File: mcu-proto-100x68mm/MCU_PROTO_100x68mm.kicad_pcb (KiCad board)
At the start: 2 copper layers, 90 x 58 mm, 333 parts, among them J1 Screw_Terminal_01x04, J10 Conn_01x20_Female, J11 Conn_01x01_Male, J12 Conn_01x01_Male, J2 Screw_Terminal_01x04, J3 Conn_01x20_Female, J4 Conn_01x20_Female, J5 Conn_01x20_Female, J6 Conn_01x20_Female, J7 Conn_01x20_Female, J8 Conn_01x20_Female, J9 Conn_01x20_Female

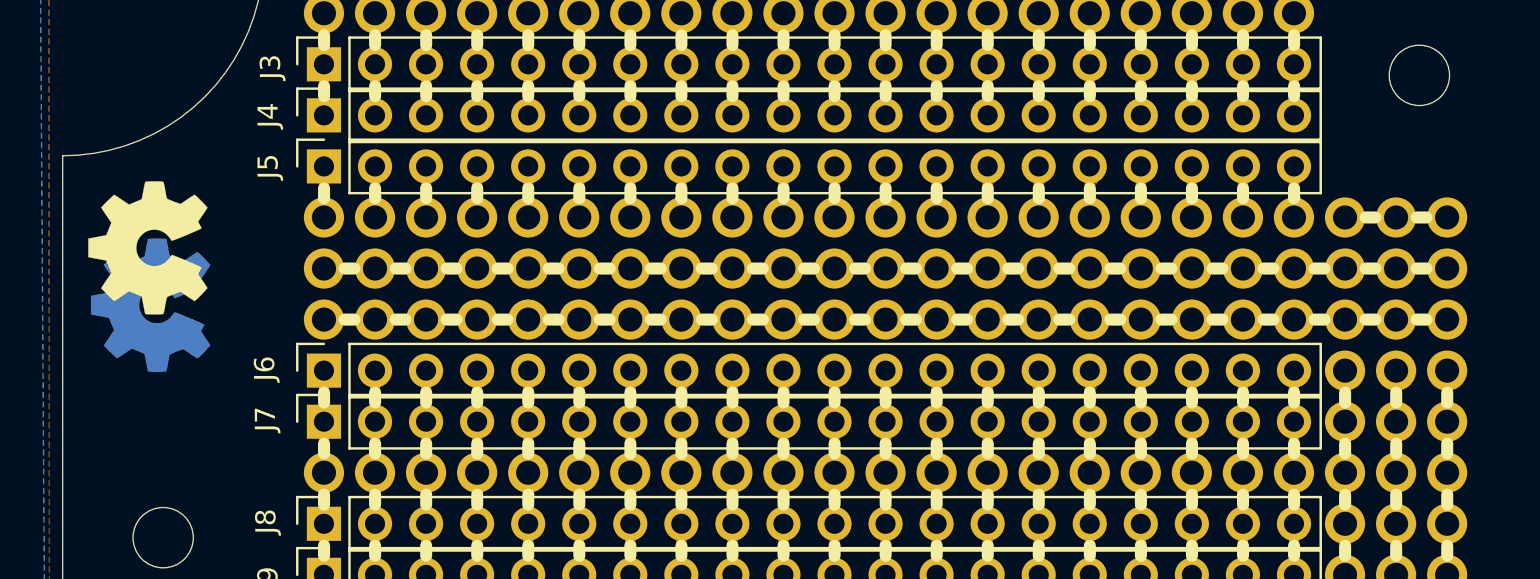
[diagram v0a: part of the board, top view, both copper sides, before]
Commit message: doc:(misistemote)changed name
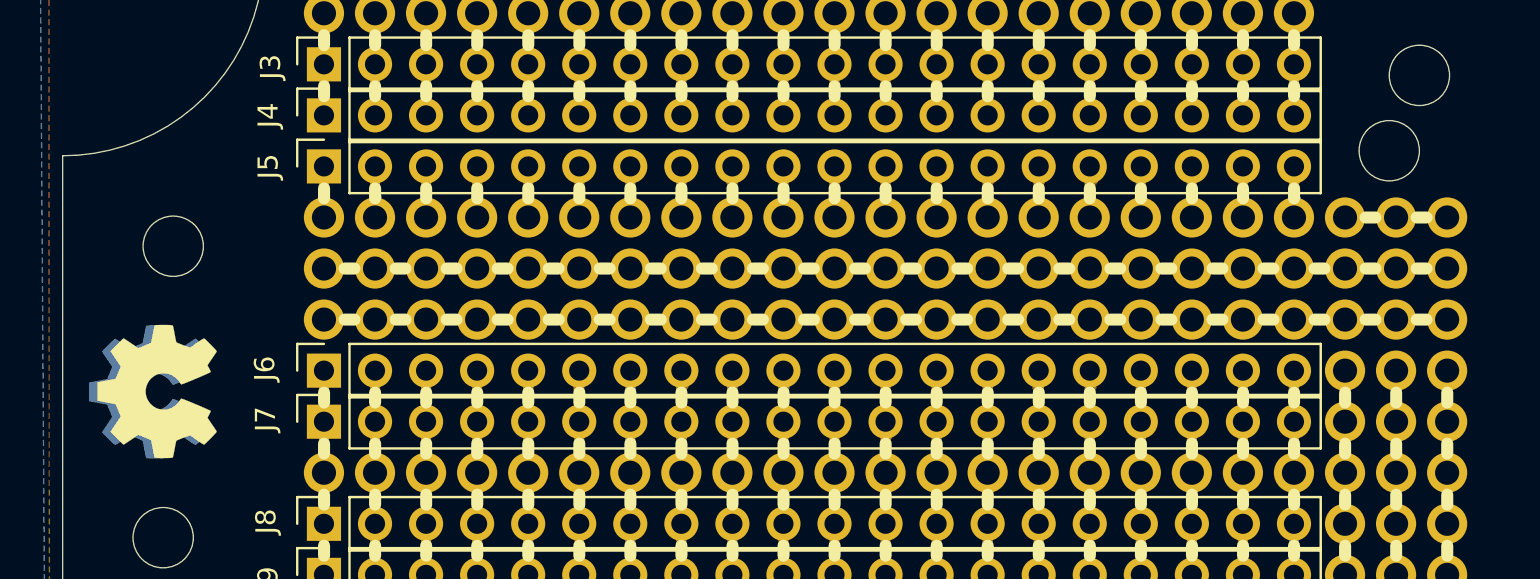
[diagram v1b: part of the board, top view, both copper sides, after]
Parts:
- added H2: MountingHole, MountingHole:MountingHole_3mm, F.Cu at (105.5, 114.5)
- added H4: MountingHole, MountingHole:MountingHole_3mm, F.Cu at (166.0, 109.8)
- moved REF** 7.16 mm to (104.7, 121.7)
- moved REF** 4.31 mm to (104.3, 121.7)
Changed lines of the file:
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@@
     (tracks 892)
     (zones 0)
-    (modules 333)
+    (modules 335)
     (nets 170)
   )
@@
     (uvia_drill 0.1)
   )
+  (module MountingHole:MountingHole_3mm (layer F.Cu)
+    (at 166 109.75)
+    (descr "Mounting Hole 3mm, no annular")
+    (tags "mounting hole 3mm no annular")
+    (attr virtual)
+    (fp_text reference H4 (at 0 -4) (layer F.SilkS) hide
+      (effects (font (size 1 1) (thickness 0.15)))
+    )
+    (fp_text value MountingHole (at 0 4) (layer F.Fab)
+      (effects (font (size 1 1) (thickness 0.15)))
+    )
+    (fp_text user %R (at 0.3 0) (layer F.Fab)
+      (effects (font (size 1 1) (thickness 0.15)))
+    )
+    (fp_circle (center 0 0) (end 3 0) (layer Cmts.User) (width 0.15))
+    (fp_circle (center 0 0) (end 3.25 0) (layer F.CrtYd) (width 0.05))
+    (pad 1 np_thru_hole circle (at 0 0) (size 3 3) (drill 3) (layers *.Cu *.Mask))
+  )
+  (module MountingHole:MountingHole_3mm (layer F.Cu)
+    (at 105.5 114.5)
+    (descr "Mounting Hole 3mm, no annular")
+    (tags "mounting hole 3mm no annular")
+    (attr virtual)
+    (fp_text reference H2 (at 0.545 2.5) (layer F.SilkS) hide
+      (effects (font (size 1 1) (thickness 0.15)))
+    )
+    (fp_text value MountingHole (at 0 4) (layer F.Fab)
+      (effects (font (size 1 1) (thickness 0.15)))
+    )
+    (fp_text user %R (at 0.3 0) (layer F.Fab)
+      (effects (font (size 1 1) (thickness 0.15)))
+    )
+    (fp_circle (center 0 0) (end 3 0) (layer Cmts.User) (width 0.15))
+    (fp_circle (center 0 0) (end 3.25 0) (layer F.CrtYd) (width 0.05))
+    (pad 1 np_thru_hole circle (at 0 0) (size 3 3) (drill 3) (layers *.Cu *.Mask))
+  )
   (module Connector_Wire:SolderWirePad_1x01_Drill0.8mm (layer F.Cu)
     (at 130.78 135.93)
@@
   )
   (module Symbol:OSHW-Symbol_6.7x6mm_SilkScreen (layer F.Cu)
-    (at 104.2543 114.5921 90)
+    (at 104.71912 121.73712 90)
     (descr "Open Source Hardware Symbol")
     (tags "Logo Symbol OSHW")
@@
   )
   (module Symbol:OSHW-Symbol_6.7x6mm_Copper (layer B.Cu)
-    (at 104.394 117.4242 270)
+    (at 104.30256 121.73712 270)
     (descr "Open Source Hardware Symbol")
     (tags "Logo Symbol OSHW")

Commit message: Minor revision update
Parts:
- removed H2 (x2), H3, H4 (x2), H5, H6: MountingHole, MountingHole:MountingHole_3mm
- removed J10, J5, J6, J7, J8, J9: Conn_01x20_Female, Connector_PinSocket_2.54mm:PinSocket_1x20_P2.54mm_Vertical
- removed J11, J12: Conn_01x01_Male, Connector_Wire:SolderWirePad_1x01_Drill0.8mm
- removed the REF** at (130.8, 135.9)
- removed the REF** at (140.9, 125.8)
- removed the REF** at (161.3, 151.2)
- removed the REF** at (158.7, 151.2)
- removed the REF** at (156.2, 151.2)
- removed the REF** at (153.6, 151.2)
- removed the REF** at (151.1, 151.2)
- removed the REF** at (148.6, 151.2)
- removed the REF** at (146.0, 151.2)
- removed the REF** at (143.5, 151.2)
- removed the REF** at (140.9, 151.2)
- removed the REF** at (138.4, 151.2)
- removed the REF** at (138.4, 125.8)
- removed the REF** at (135.9, 151.2)
- removed the REF** at (133.3, 151.2)
- removed the REF** at (130.8, 151.2)
- removed the REF** at (128.2, 151.2)
- removed the REF** at (161.3, 148.6)
- removed the REF** at (158.7, 148.6)
- removed the REF** at (156.2, 148.6)
- removed the REF** at (153.6, 148.6)
- removed the REF** at (151.1, 148.6)
- removed the REF** at (148.6, 148.6)
- removed the REF** at (135.9, 125.8)
- removed the REF** at (146.0, 148.6)
- removed the REF** at (143.5, 148.6)
- removed the REF** at (140.9, 148.6)
- removed the REF** at (138.4, 148.6)
- removed the REF** at (135.9, 148.6)
- removed the REF** at (133.3, 148.6)
- removed the REF** at (130.8, 148.6)
- removed the REF** at (128.2, 148.6)
- removed the REF** at (115.5, 156.2)
- removed the REF** at (113.0, 156.2)
- removed the REF** at (133.3, 125.8)
- removed the REF** at (115.5, 153.7)
- removed the REF** at (113.0, 153.7)
- removed the REF** at (115.5, 151.2)
- removed the REF** at (113.0, 151.2)
- removed the REF** at (115.5, 148.6)
- removed the REF** at (113.0, 148.6)
- removed the REF** at (161.3, 146.1)
- removed the REF** at (158.7, 146.1)
- removed the REF** at (156.2, 146.1)
- removed the REF** at (153.6, 146.1)
- removed the REF** at (130.8, 125.8)
- removed the REF** at (151.1, 146.1)
- removed the REF** at (148.6, 146.1)
- removed the REF** at (146.0, 146.1)
- removed the REF** at (143.5, 146.1)
- removed the REF** at (140.9, 146.1)
- removed the REF** at (138.4, 146.1)
- removed the REF** at (135.9, 146.1)
- removed the REF** at (133.3, 146.1)
- removed the REF** at (130.8, 146.1)
- removed the REF** at (128.2, 146.1)
- removed the REF** at (128.2, 125.8)
- removed the REF** at (125.7, 146.1)
- removed the REF** at (123.2, 146.1)
- removed the REF** at (120.6, 146.1)
- removed the REF** at (118.1, 146.1)
- removed the REF** at (115.5, 146.1)
- removed the REF** at (113.0, 146.1)
- removed the REF** at (161.3, 143.6)
- removed the REF** at (158.7, 143.6)
- removed the REF** at (156.2, 143.6)
- removed the REF** at (153.6, 143.6)
- removed the REF** at (125.7, 125.8)
- removed the REF** at (151.1, 143.6)
- removed the REF** at (148.6, 143.6)
- removed the REF** at (146.0, 143.6)
- removed the REF** at (143.5, 143.6)
- removed the REF** at (140.9, 143.6)
- removed the REF** at (138.4, 143.6)
- removed the REF** at (135.9, 143.6)
- removed the REF** at (133.3, 143.6)
- removed the REF** at (130.8, 143.6)
- removed the REF** at (128.2, 143.6)
- removed the REF** at (123.2, 125.8)
- removed the REF** at (125.7, 143.6)
- removed the REF** at (123.2, 143.6)
- removed the REF** at (120.6, 143.6)
- removed the REF** at (118.1, 143.6)
- removed the REF** at (115.5, 143.6)
- removed the REF** at (113.0, 143.6)
- removed the REF** at (161.3, 141.0)
- removed the REF** at (158.7, 141.0)
- removed the REF** at (156.2, 141.0)
- removed the REF** at (153.6, 141.0)
- removed the REF** at (120.6, 125.8)
- removed the REF** at (151.1, 141.0)
- removed the REF** at (148.6, 141.0)
- removed the REF** at (146.0, 141.0)
- removed the REF** at (143.5, 141.0)
- removed the REF** at (140.9, 141.0)
- removed the REF** at (138.4, 141.0)
- removed the REF** at (135.9, 141.0)
- removed the REF** at (133.3, 141.0)
- removed the REF** at (130.8, 141.0)
- removed the REF** at (128.2, 141.0)
- removed the REF** at (118.1, 125.8)
- removed the REF** at (125.7, 141.0)
- removed the REF** at (123.2, 141.0)
- removed the REF** at (120.6, 141.0)
- removed the REF** at (118.1, 141.0)
- removed the REF** at (115.5, 141.0)
- removed the REF** at (113.0, 141.0)
- removed the REF** at (161.3, 138.5)
- removed the REF** at (158.7, 138.5)
- removed the REF** at (156.2, 138.5)
- removed the REF** at (153.6, 138.5)
- removed the REF** at (161.3, 125.8)
- removed the REF** at (115.5, 125.8)
- removed the REF** at (151.1, 138.5)
- removed the REF** at (148.6, 138.5)
- removed the REF** at (146.0, 138.5)
- removed the REF** at (143.5, 138.5)
- removed the REF** at (140.9, 138.5)
- removed the REF** at (138.4, 138.5)
- removed the REF** at (135.9, 138.5)
- removed the REF** at (133.3, 138.5)
- removed the REF** at (130.8, 138.5)
- removed the REF** at (128.2, 138.5)
- removed the REF** at (113.0, 125.8)
- removed the REF** at (125.7, 138.5)
- removed the REF** at (123.2, 138.5)
- removed the REF** at (120.6, 138.5)
- removed the REF** at (118.1, 138.5)
- removed the REF** at (115.5, 138.5)
- removed the REF** at (113.0, 138.5)
- removed the REF** at (161.3, 135.9)
- removed the REF** at (158.7, 135.9)
- removed the REF** at (156.2, 135.9)
- removed the REF** at (153.6, 135.9)
- removed the REF** at (174.5, 121.5)
- removed the REF** at (151.1, 135.9)
- removed the REF** at (148.6, 135.9)
- removed the REF** at (146.0, 135.9)
- removed the REF** at (143.5, 135.9)
- removed the REF** at (140.9, 135.9)
- removed the REF** at (138.4, 135.9)
- removed the REF** at (135.9, 135.9)
- removed the REF** at (133.3, 135.9)
- removed the REF** at (128.2, 135.9)
- removed the REF** at (125.7, 135.9)
- removed the REF** at (174.5, 118.0)
- removed the REF** at (123.2, 135.9)
- removed the REF** at (120.6, 135.9)
- removed the REF** at (118.1, 135.9)
- removed the REF** at (115.5, 135.9)
- removed the REF** at (161.3, 118.2)
- removed the REF** at (158.7, 118.2)
- removed the REF** at (156.2, 118.2)
- removed the REF** at (153.6, 118.2)
- removed the REF** at (151.1, 118.2)
- removed the REF** at (148.6, 118.2)
- removed the REF** at (174.5, 114.5)
- removed the REF** at (146.0, 118.2)
- removed the REF** at (143.5, 118.2)
- removed the REF** at (140.9, 118.2)
- removed the REF** at (138.4, 118.2)
- removed the REF** at (135.9, 118.2)
- removed the REF** at (133.3, 118.2)
- removed the REF** at (130.8, 118.2)
- removed the REF** at (128.2, 118.2)
- removed the REF** at (125.7, 118.2)
- removed the REF** at (123.2, 118.2)
- removed the REF** at (174.5, 111.0)
- removed the REF** at (120.6, 118.2)
- removed the REF** at (118.1, 118.2)
- removed the REF** at (115.5, 118.2)
- removed the REF** at (113.0, 118.2)
- removed the REF** at (161.3, 115.6)
- removed the REF** at (158.7, 115.6)
- removed the REF** at (156.2, 115.6)
- removed the REF** at (153.6, 115.6)
- removed the REF** at (151.1, 115.6)
- removed the REF** at (148.6, 115.6)
- removed the REF** at (168.9, 133.4)
- removed the REF** at (146.0, 115.6)
- removed the REF** at (143.5, 115.6)
- removed the REF** at (140.9, 115.6)
- removed the REF** at (138.4, 115.6)
- removed the REF** at (135.9, 115.6)
- removed the REF** at (133.3, 115.6)
- removed the REF** at (130.8, 115.6)
- removed the REF** at (128.2, 115.6)
- removed the REF** at (125.7, 115.6)
- removed the REF** at (123.2, 115.6)
- removed the REF** at (166.3, 133.4)
- removed the REF** at (120.6, 115.6)
- removed the REF** at (118.1, 115.6)
- removed the REF** at (115.5, 115.6)
- removed the REF** at (113.0, 115.6)
- removed the REF** at (161.3, 113.1)
- removed the REF** at (158.7, 113.1)
- removed the REF** at (156.2, 113.1)
- removed the REF** at (153.6, 113.1)
- removed the REF** at (151.1, 113.1)
- removed the REF** at (148.6, 113.1)
- removed the REF** at (163.8, 133.4)
- removed the REF** at (146.0, 113.1)
- removed the REF** at (143.5, 113.1)
- removed the REF** at (140.9, 113.1)
- removed the REF** at (138.4, 113.1)
- removed the REF** at (135.9, 113.1)
- removed the REF** at (133.3, 113.1)
- removed the REF** at (130.8, 113.1)
- removed the REF** at (128.2, 113.1)
- removed the REF** at (125.7, 113.1)
- removed the REF** at (123.2, 113.1)
- removed the REF** at (168.9, 130.8)
- removed the REF** at (120.6, 113.1)
- removed the REF** at (118.1, 113.1)
- removed the REF** at (115.5, 113.1)
- removed the REF** at (113.0, 113.1)
- removed the REF** at (113.0, 135.9)
- removed the REF** at (113.0, 102.9)
- removed the REF** at (115.5, 102.9)
- removed the REF** at (118.1, 102.9)
- removed the REF** at (120.6, 102.9)
- removed the REF** at (123.2, 102.9)
- removed the REF** at (158.7, 125.8)
- removed the REF** at (166.3, 130.8)
- removed the REF** at (125.7, 102.9)
- removed the REF** at (148.6, 102.9)
- removed the REF** at (161.3, 102.9)
- removed the REF** at (158.7, 102.9)
- removed the REF** at (156.2, 102.9)
- removed the REF** at (153.6, 102.9)
- removed the REF** at (151.1, 102.9)
- removed the REF** at (146.0, 102.9)
- removed the REF** at (143.5, 102.9)
- removed the REF** at (140.9, 102.9)
- removed the REF** at (163.8, 130.8)
- removed the REF** at (138.4, 102.9)
- removed the REF** at (135.9, 102.9)
- removed the REF** at (133.3, 102.9)
- removed the REF** at (130.8, 102.9)
- removed the REF** at (128.2, 102.9)
- removed the REF** at (168.9, 128.3)
- removed the REF** at (166.3, 128.3)
- removed the REF** at (163.8, 128.3)
- removed the REF** at (168.9, 125.8)
- removed the REF** at (166.3, 125.8)
- removed the REF** at (163.8, 125.8)
- removed the REF** at (168.9, 123.2)
- removed the REF** at (166.3, 123.2)
- removed the REF** at (156.2, 125.8)
- removed the REF** at (163.8, 123.2)
- removed the REF** at (168.9, 120.7)
- removed the REF** at (166.3, 120.7)
- removed the REF** at (163.8, 120.7)
- removed the REF** at (168.9, 118.2)
- removed the REF** at (166.3, 118.2)
- removed the REF** at (163.8, 118.2)
- removed the REF** at (168.9, 115.6)
- removed the REF** at (166.3, 115.6)
- removed the REF** at (163.8, 115.6)
- removed the REF** at (153.6, 125.8)
- removed the REF** at (168.9, 113.1)
- removed the REF** at (166.3, 113.1)
- removed the REF** at (163.8, 113.1)
- removed the REF** at (174.5, 147.0)
- removed the REF** at (168.9, 146.1)
- removed the REF** at (166.3, 146.1)
- removed the REF** at (163.8, 146.1)
- removed the REF** at (174.5, 143.5)
- removed the REF** at (168.9, 143.6)
- removed the REF** at (166.3, 143.6)
- removed the REF** at (151.1, 125.8)
- removed the REF** at (163.8, 143.6)
- removed the REF** at (174.5, 140.0)
- removed the REF** at (168.9, 141.0)
- removed the REF** at (166.3, 141.0)
- removed the REF** at (163.8, 141.0)
- removed the REF** at (174.5, 136.5)
- removed the REF** at (168.9, 138.5)
- removed the REF** at (166.3, 138.5)
- removed the REF** at (163.8, 138.5)
- removed the REF** at (168.9, 135.9)
- removed the REF** at (148.6, 125.8)
- removed the REF** at (166.3, 135.9)
- removed the REF** at (163.8, 135.9)
- removed the REF** at (161.3, 156.2)
- removed the REF** at (158.7, 156.2)
- removed the REF** at (156.2, 156.2)
- removed the REF** at (153.6, 156.2)
- removed the REF** at (151.1, 156.2)
- removed the REF** at (148.6, 156.2)
- removed the REF** at (146.0, 156.2)
- removed the REF** at (143.5, 156.2)
- removed the REF** at (146.0, 125.8)
- removed the REF** at (140.9, 156.2)
- removed the REF** at (138.4, 156.2)
- removed the REF** at (135.9, 156.2)
- removed the REF** at (133.3, 156.2)
- removed the REF** at (130.8, 156.2)
- removed the REF** at (128.2, 156.2)
- removed the REF** at (161.3, 153.7)
- removed the REF** at (158.7, 153.7)
- removed the REF** at (156.2, 153.7)
- removed the REF** at (153.6, 153.7)
- removed the REF** at (143.5, 125.8)
- removed the REF** at (151.1, 153.7)
- removed the REF** at (148.6, 153.7)
- removed the REF** at (146.0, 153.7)
- removed the REF** at (143.5, 153.7)
- removed the REF** at (140.9, 153.7)
- removed the REF** at (138.4, 153.7)
- removed the REF** at (135.9, 153.7)
- removed the REF** at (133.3, 153.7)
- removed the REF** at (130.8, 153.7)
- removed the REF** at (128.2, 153.7)
- added REF**: Round_Pad_1.7mm_Hole_1.0mm, proto-pcb-pads:RoundPad_1.7mm_Hole_1.0mm, F.Cu at (130.8, 153.7)
- added REF**: Round_Pad_1.7mm_Hole_1.0mm, proto-pcb-pads:RoundPad_1.7mm_Hole_1.0mm, F.Cu at (118.1, 110.5)
- added REF**: Round_Pad_1.7mm_Hole_1.0mm, proto-pcb-pads:RoundPad_1.7mm_Hole_1.0mm, F.Cu at (158.7, 141.0)
- added REF**: Round_Pad_1.7mm_Hole_1.0mm, proto-pcb-pads:RoundPad_1.7mm_Hole_1.0mm, F.Cu at (153.6, 135.9)
- added REF**: Round_Pad_1.7mm_Hole_1.0mm, proto-pcb-pads:RoundPad_1.7mm_Hole_1.0mm, F.Cu at (163.8, 123.2)
- added REF**: Round_Pad_1.7mm_Hole_1.0mm, proto-pcb-pads:RoundPad_1.7mm_Hole_1.0mm, F.Cu at (125.7, 128.3)
- added REF**: Round_Pad_1.7mm_Hole_1.0mm, proto-pcb-pads:RoundPad_1.7mm_Hole_1.0mm, F.Cu at (148.6, 141.0)
- added REF**: Round_Pad_1.7mm_Hole_1.0mm, proto-pcb-pads:RoundPad_1.7mm_Hole_1.0mm, F.Cu at (153.6, 115.6)
- added REF**: Round_Pad_1.7mm_Hole_1.0mm, proto-pcb-pads:RoundPad_1.7mm_Hole_1.0mm, F.Cu at (143.5, 108.0)
- added REF**: Round_Pad_1.7mm_Hole_1.0mm, proto-pcb-pads:RoundPad_1.7mm_Hole_1.0mm, F.Cu at (161.3, 130.8)
- added REF**: Round_Pad_1.7mm_Hole_1.0mm, proto-pcb-pads:RoundPad_1.7mm_Hole_1.0mm, F.Cu at (115.5, 135.9)
- added REF**: Round_Pad_1.7mm_Hole_1.0mm, proto-pcb-pads:RoundPad_1.7mm_Hole_1.0mm, F.Cu at (153.6, 130.8)
- added REF**: Round_Pad_1.7mm_Hole_1.0mm, proto-pcb-pads:RoundPad_1.7mm_Hole_1.0mm, F.Cu at (133.3, 115.6)
- added REF**: Round_Pad_1.7mm_Hole_1.0mm, proto-pcb-pads:RoundPad_1.7mm_Hole_1.0mm, F.Cu at (120.6, 128.3)
- added REF**: Round_Pad_1.7mm_Hole_1.0mm, proto-pcb-pads:RoundPad_1.7mm_Hole_1.0mm, F.Cu at (130.8, 151.2)
- added REF**: Round_Pad_1.7mm_Hole_1.0mm, proto-pcb-pads:RoundPad_1.7mm_Hole_1.0mm, F.Cu at (130.8, 146.1)
- added REF**: Round_Pad_1.7mm_Hole_1.0mm, proto-pcb-pads:RoundPad_1.7mm_Hole_1.0mm, F.Cu at (146.0, 138.5)
- added REF**: Round_Pad_1.7mm_Hole_1.0mm, proto-pcb-pads:RoundPad_1.7mm_Hole_1.0mm, F.Cu at (143.5, 128.3)
- added REF**: Round_Pad_1.7mm_Hole_1.0mm, proto-pcb-pads:RoundPad_1.7mm_Hole_1.0mm, F.Cu at (146.0, 128.3)
- added REF**: Round_Pad_1.7mm_Hole_1.0mm, proto-pcb-pads:RoundPad_1.7mm_Hole_1.0mm, F.Cu at (140.9, 130.8)
- added REF**: Round_Pad_1.7mm_Hole_1.0mm, proto-pcb-pads:RoundPad_1.7mm_Hole_1.0mm, F.Cu at (115.5, 138.5)
- added REF**: Round_Pad_1.7mm_Hole_1.0mm, proto-pcb-pads:RoundPad_1.7mm_Hole_1.0mm, F.Cu at (113.0, 115.6)
- added REF**: Round_Pad_1.7mm_Hole_1.0mm, proto-pcb-pads:RoundPad_1.7mm_Hole_1.0mm, F.Cu at (163.8, 120.7)
- added REF**: Round_Pad_1.7mm_Hole_1.0mm, proto-pcb-pads:RoundPad_1.7mm_Hole_1.0mm, F.Cu at (140.9, 148.6)
- added REF**: Round_Pad_1.7mm_Hole_1.0mm, proto-pcb-pads:RoundPad_1.7mm_Hole_1.0mm, F.Cu at (133.3, 120.7)
- added REF**: Round_Pad_1.7mm_Hole_1.0mm, proto-pcb-pads:RoundPad_1.7mm_Hole_1.0mm, F.Cu at (113.0, 133.4)
- added REF**: Round_Pad_1.7mm_Hole_1.0mm, proto-pcb-pads:RoundPad_1.7mm_Hole_1.0mm, F.Cu at (125.7, 120.7)
- added REF**: Round_Pad_1.7mm_Hole_1.0mm, proto-pcb-pads:RoundPad_1.7mm_Hole_1.0mm, F.Cu at (151.1, 153.7)
- added REF**: Round_Pad_1.7mm_Hole_1.0mm, proto-pcb-pads:RoundPad_1.7mm_Hole_1.0mm, F.Cu at (125.7, 138.5)
- added REF**: Round_Pad_1.7mm_Hole_1.0mm, proto-pcb-pads:RoundPad_1.7mm_Hole_1.0mm, F.Cu at (130.8, 123.2)
- added REF**: Round_Pad_1.7mm_Hole_1.0mm, proto-pcb-pads:RoundPad_1.7mm_Hole_1.0mm, F.Cu at (128.2, 123.2)
- added REF**: Round_Pad_1.7mm_Hole_1.0mm, proto-pcb-pads:RoundPad_1.7mm_Hole_1.0mm, F.Cu at (174.5, 111.0)
- added REF**: Round_Pad_1.7mm_Hole_1.0mm, proto-pcb-pads:RoundPad_1.7mm_Hole_1.0mm, F.Cu at (133.3, 138.5)
- added REF**: Round_Pad_1.7mm_Hole_1.0mm, proto-pcb-pads:RoundPad_1.7mm_Hole_1.0mm, F.Cu at (161.3, 135.9)
- added REF**: Round_Pad_1.7mm_Hole_1.0mm, proto-pcb-pads:RoundPad_1.7mm_Hole_1.0mm, F.Cu at (133.3, 102.9)
- added REF**: Round_Pad_1.7mm_Hole_1.0mm, proto-pcb-pads:RoundPad_1.7mm_Hole_1.0mm, F.Cu at (123.2, 146.1)
- added REF**: Round_Pad_1.7mm_Hole_1.0mm, proto-pcb-pads:RoundPad_1.7mm_Hole_1.0mm, F.Cu at (138.4, 102.9)
- added REF**: Round_Pad_1.7mm_Hole_1.0mm, proto-pcb-pads:RoundPad_1.7mm_Hole_1.0mm, F.Cu at (146.0, 156.2)
- added REF**: Round_Pad_1.7mm_Hole_1.0mm, proto-pcb-pads:RoundPad_1.7mm_Hole_1.0mm, F.Cu at (123.2, 115.6)
- added REF**: Round_Pad_1.7mm_Hole_1.0mm, proto-pcb-pads:RoundPad_1.7mm_Hole_1.0mm, F.Cu at (151.1, 105.5)
- added REF**: Round_Pad_1.7mm_Hole_1.0mm, proto-pcb-pads:RoundPad_1.7mm_Hole_1.0mm, F.Cu at (123.2, 125.8)
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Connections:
- J1 pad 1: Net-(J1-Pad1) -> unconnected-(J1-Pin_1-Pad1)
- J1 pad 2: Net-(J1-Pad2) -> unconnected-(J1-Pin_2-Pad2)
- J1 pad 3: Net-(J1-Pad3) -> unconnected-(J1-Pin_3-Pad3)
- J1 pad 4: Net-(J1-Pad4) -> unconnected-(J1-Pin_4-Pad4)
- J2 pad 1: Net-(J2-Pad1) -> unconnected-(J2-Pin_1-Pad1)
- J2 pad 2: Net-(J2-Pad2) -> unconnected-(J2-Pin_2-Pad2)
- J2 pad 3: Net-(J2-Pad3) -> unconnected-(J2-Pin_3-Pad3)
- J2 pad 4: Net-(J2-Pad4) -> unconnected-(J2-Pin_4-Pad4)
- J3 pad 1: Net-(J3-Pad1) -> Net-(J3-Pin_1)
- J4 pad 1: Net-(J4-Pad1) -> Net-(J3-Pin_1)
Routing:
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- removed copper zone on B.Cu, net Net-(J11-Pad1)
- removed copper zone on F.Cu, net Net-(J11-Pad1)
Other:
- net class Default removed
- net class slimstack removed
- board text added: "GND"

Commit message: Silkscreen on front side
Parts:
- added REF**: Pad_Link_1.7mm_Width_1.0mm, proto-pcb-silks:PadLink_1.7mm_Width_1.0mm, F.Cu at (113.0, 105.5)
- added REF**1: Pad_Link_1.7mm_Width_1.0mm, proto-pcb-silks:PadLink_1.7mm_Width_1.0mm, F.Cu at (115.5, 105.5)
- added REF**10: Pad_Link_1.7mm_Width_1.0mm, proto-pcb-silks:PadLink_1.7mm_Width_1.0mm, F.Cu at (138.4, 105.5)
- added REF**100: Pad_Link_1.7mm_Width_1.0mm, proto-pcb-silks:PadLink_1.7mm_Width_1.0mm, F.Cu at (163.8, 118.2)
- added REF**101: Pad_Link_1.7mm_Width_1.0mm, proto-pcb-silks:PadLink_1.7mm_Width_1.0mm, F.Cu at (166.3, 118.2)
- added REF**102: Pad_Link_1.7mm_Width_1.0mm, proto-pcb-silks:PadLink_1.7mm_Width_1.0mm, F.Cu at (163.8, 113.1)
- added REF**103: Pad_Link_1.7mm_Width_1.0mm, proto-pcb-silks:PadLink_1.7mm_Width_1.0mm, F.Cu at (166.3, 113.1)
- added REF**104: Pad_Link_1.7mm_Width_1.0mm, proto-pcb-silks:PadLink_1.7mm_Width_1.0mm, F.Cu at (113.0, 123.2)
- added REF**105: Pad_Link_1.7mm_Width_1.0mm, proto-pcb-silks:PadLink_1.7mm_Width_1.0mm, F.Cu at (115.5, 123.2)
- added REF**106: Pad_Link_1.7mm_Width_1.0mm, proto-pcb-silks:PadLink_1.7mm_Width_1.0mm, F.Cu at (118.1, 123.2)
- added REF**107: Pad_Link_1.7mm_Width_1.0mm, proto-pcb-silks:PadLink_1.7mm_Width_1.0mm, F.Cu at (120.6, 123.2)
- added REF**108: Pad_Link_1.7mm_Width_1.0mm, proto-pcb-silks:PadLink_1.7mm_Width_1.0mm, F.Cu at (123.2, 123.2)
- added REF**109: Pad_Link_1.7mm_Width_1.0mm, proto-pcb-silks:PadLink_1.7mm_Width_1.0mm, F.Cu at (125.7, 123.2)
- added REF**11: Pad_Link_1.7mm_Width_1.0mm, proto-pcb-silks:PadLink_1.7mm_Width_1.0mm, F.Cu at (140.9, 105.5)
- added REF**110: Pad_Link_1.7mm_Width_1.0mm, proto-pcb-silks:PadLink_1.7mm_Width_1.0mm, F.Cu at (128.2, 123.2)
- added REF**111: Pad_Link_1.7mm_Width_1.0mm, proto-pcb-silks:PadLink_1.7mm_Width_1.0mm, F.Cu at (130.8, 123.2)
- added REF**112: Pad_Link_1.7mm_Width_1.0mm, proto-pcb-silks:PadLink_1.7mm_Width_1.0mm, F.Cu at (133.3, 123.2)
- added REF**113: Pad_Link_1.7mm_Width_1.0mm, proto-pcb-silks:PadLink_1.7mm_Width_1.0mm, F.Cu at (135.9, 123.2)
- added REF**114: Pad_Link_1.7mm_Width_1.0mm, proto-pcb-silks:PadLink_1.7mm_Width_1.0mm, F.Cu at (138.4, 123.2)
- added REF**115: Pad_Link_1.7mm_Width_1.0mm, proto-pcb-silks:PadLink_1.7mm_Width_1.0mm, F.Cu at (140.9, 123.2)
- added REF**116: Pad_Link_1.7mm_Width_1.0mm, proto-pcb-silks:PadLink_1.7mm_Width_1.0mm, F.Cu at (143.5, 123.2)
- added REF**117: Pad_Link_1.7mm_Width_1.0mm, proto-pcb-silks:PadLink_1.7mm_Width_1.0mm, F.Cu at (146.0, 123.2)
- added REF**118: Pad_Link_1.7mm_Width_1.0mm, proto-pcb-silks:PadLink_1.7mm_Width_1.0mm, F.Cu at (148.6, 123.2)
- added REF**119: Pad_Link_1.7mm_Width_1.0mm, proto-pcb-silks:PadLink_1.7mm_Width_1.0mm, F.Cu at (151.1, 123.2)
- added REF**12: Pad_Link_1.7mm_Width_1.0mm, proto-pcb-silks:PadLink_1.7mm_Width_1.0mm, F.Cu at (143.5, 105.5)
- added REF**120: Pad_Link_1.7mm_Width_1.0mm, proto-pcb-silks:PadLink_1.7mm_Width_1.0mm, F.Cu at (153.6, 123.2)
- added REF**121: Pad_Link_1.7mm_Width_1.0mm, proto-pcb-silks:PadLink_1.7mm_Width_1.0mm, F.Cu at (156.2, 123.2)
- added REF**122: Pad_Link_1.7mm_Width_1.0mm, proto-pcb-silks:PadLink_1.7mm_Width_1.0mm, F.Cu at (158.7, 123.2)
- added REF**123: Pad_Link_1.7mm_Width_1.0mm, proto-pcb-silks:PadLink_1.7mm_Width_1.0mm, F.Cu at (161.3, 123.2)
- added REF**124: Pad_Link_1.7mm_Width_1.0mm, proto-pcb-silks:PadLink_1.7mm_Width_1.0mm, F.Cu at (163.8, 123.2)
- added REF**125: Pad_Link_1.7mm_Width_1.0mm, proto-pcb-silks:PadLink_1.7mm_Width_1.0mm, F.Cu at (166.3, 123.2)
- added REF**126: Pad_Link_1.7mm_Width_1.0mm, proto-pcb-silks:PadLink_1.7mm_Width_1.0mm, F.Cu at (168.9, 123.2)
- added REF**127: Pad_Link_1.7mm_Width_1.0mm, proto-pcb-silks:PadLink_1.7mm_Width_1.0mm, F.Cu at (113.0, 125.8)
- added REF**128: Pad_Link_1.7mm_Width_1.0mm, proto-pcb-silks:PadLink_1.7mm_Width_1.0mm, F.Cu at (115.5, 125.8)
- added REF**129: Pad_Link_1.7mm_Width_1.0mm, proto-pcb-silks:PadLink_1.7mm_Width_1.0mm, F.Cu at (118.1, 125.8)
- added REF**13: Pad_Link_1.7mm_Width_1.0mm, proto-pcb-silks:PadLink_1.7mm_Width_1.0mm, F.Cu at (146.0, 105.5)
- added REF**130: Pad_Link_1.7mm_Width_1.0mm, proto-pcb-silks:PadLink_1.7mm_Width_1.0mm, F.Cu at (120.6, 125.8)
- added REF**131: Pad_Link_1.7mm_Width_1.0mm, proto-pcb-silks:PadLink_1.7mm_Width_1.0mm, F.Cu at (123.2, 125.8)
- added REF**132: Pad_Link_1.7mm_Width_1.0mm, proto-pcb-silks:PadLink_1.7mm_Width_1.0mm, F.Cu at (125.7, 125.8)
- added REF**133: Pad_Link_1.7mm_Width_1.0mm, proto-pcb-silks:PadLink_1.7mm_Width_1.0mm, F.Cu at (128.2, 125.8)
- added REF**134: Pad_Link_1.7mm_Width_1.0mm, proto-pcb-silks:PadLink_1.7mm_Width_1.0mm, F.Cu at (130.8, 125.8)
- added REF**135: Pad_Link_1.7mm_Width_1.0mm, proto-pcb-silks:PadLink_1.7mm_Width_1.0mm, F.Cu at (133.3, 125.8)
- added REF**136: Pad_Link_1.7mm_Width_1.0mm, proto-pcb-silks:PadLink_1.7mm_Width_1.0mm, F.Cu at (135.9, 125.8)
- added REF**137: Pad_Link_1.7mm_Width_1.0mm, proto-pcb-silks:PadLink_1.7mm_Width_1.0mm, F.Cu at (138.4, 125.8)
- added REF**138: Pad_Link_1.7mm_Width_1.0mm, proto-pcb-silks:PadLink_1.7mm_Width_1.0mm, F.Cu at (140.9, 125.8)
- added REF**139: Pad_Link_1.7mm_Width_1.0mm, proto-pcb-silks:PadLink_1.7mm_Width_1.0mm, F.Cu at (143.5, 125.8)
- added REF**14: Pad_Link_1.7mm_Width_1.0mm, proto-pcb-silks:PadLink_1.7mm_Width_1.0mm, F.Cu at (148.6, 105.5)
- added REF**140: Pad_Link_1.7mm_Width_1.0mm, proto-pcb-silks:PadLink_1.7mm_Width_1.0mm, F.Cu at (146.0, 125.8)
- added REF**141: Pad_Link_1.7mm_Width_1.0mm, proto-pcb-silks:PadLink_1.7mm_Width_1.0mm, F.Cu at (148.6, 125.8)
- added REF**142: Pad_Link_1.7mm_Width_1.0mm, proto-pcb-silks:PadLink_1.7mm_Width_1.0mm, F.Cu at (151.1, 125.8)
- added REF**143: Pad_Link_1.7mm_Width_1.0mm, proto-pcb-silks:PadLink_1.7mm_Width_1.0mm, F.Cu at (153.6, 125.8)
- added REF**144: Pad_Link_1.7mm_Width_1.0mm, proto-pcb-silks:PadLink_1.7mm_Width_1.0mm, F.Cu at (156.2, 125.8)
- added REF**145: Pad_Link_1.7mm_Width_1.0mm, proto-pcb-silks:PadLink_1.7mm_Width_1.0mm, F.Cu at (158.7, 125.8)
- added REF**146: Pad_Link_1.7mm_Width_1.0mm, proto-pcb-silks:PadLink_1.7mm_Width_1.0mm, F.Cu at (161.3, 125.8)
- added REF**147: Pad_Link_1.7mm_Width_1.0mm, proto-pcb-silks:PadLink_1.7mm_Width_1.0mm, F.Cu at (163.8, 125.8)
- added REF**148: Pad_Link_1.7mm_Width_1.0mm, proto-pcb-silks:PadLink_1.7mm_Width_1.0mm, F.Cu at (166.3, 125.8)
- added REF**149: Pad_Link_1.7mm_Width_1.0mm, proto-pcb-silks:PadLink_1.7mm_Width_1.0mm, F.Cu at (168.9, 125.8)
- added REF**15: Pad_Link_1.7mm_Width_1.0mm, proto-pcb-silks:PadLink_1.7mm_Width_1.0mm, F.Cu at (151.1, 105.5)
- added REF**150: Pad_Link_1.7mm_Width_1.0mm, proto-pcb-silks:PadLink_1.7mm_Width_1.0mm, F.Cu at (113.0, 128.3)
- added REF**151: Pad_Link_1.7mm_Width_1.0mm, proto-pcb-silks:PadLink_1.7mm_Width_1.0mm, F.Cu at (115.5, 128.3)
- added REF**152: Pad_Link_1.7mm_Width_1.0mm, proto-pcb-silks:PadLink_1.7mm_Width_1.0mm, F.Cu at (118.1, 128.3)
- added REF**153: Pad_Link_1.7mm_Width_1.0mm, proto-pcb-silks:PadLink_1.7mm_Width_1.0mm, F.Cu at (120.6, 128.3)
- added REF**154: Pad_Link_1.7mm_Width_1.0mm, proto-pcb-silks:PadLink_1.7mm_Width_1.0mm, F.Cu at (123.2, 128.3)
- added REF**155: Pad_Link_1.7mm_Width_1.0mm, proto-pcb-silks:PadLink_1.7mm_Width_1.0mm, F.Cu at (125.7, 128.3)
- added REF**156: Pad_Link_1.7mm_Width_1.0mm, proto-pcb-silks:PadLink_1.7mm_Width_1.0mm, F.Cu at (128.2, 128.3)
- added REF**157: Pad_Link_1.7mm_Width_1.0mm, proto-pcb-silks:PadLink_1.7mm_Width_1.0mm, F.Cu at (130.8, 128.3)
- added REF**158: Pad_Link_1.7mm_Width_1.0mm, proto-pcb-silks:PadLink_1.7mm_Width_1.0mm, F.Cu at (133.3, 128.3)
- added REF**159: Pad_Link_1.7mm_Width_1.0mm, proto-pcb-silks:PadLink_1.7mm_Width_1.0mm, F.Cu at (135.9, 128.3)
- added REF**16: Pad_Link_1.7mm_Width_1.0mm, proto-pcb-silks:PadLink_1.7mm_Width_1.0mm, F.Cu at (153.6, 105.5)
- added REF**160: Pad_Link_1.7mm_Width_1.0mm, proto-pcb-silks:PadLink_1.7mm_Width_1.0mm, F.Cu at (138.4, 128.3)
- added REF**161: Pad_Link_1.7mm_Width_1.0mm, proto-pcb-silks:PadLink_1.7mm_Width_1.0mm, F.Cu at (140.9, 128.3)
- added REF**162: Pad_Link_1.7mm_Width_1.0mm, proto-pcb-silks:PadLink_1.7mm_Width_1.0mm, F.Cu at (143.5, 128.3)
- added REF**163: Pad_Link_1.7mm_Width_1.0mm, proto-pcb-silks:PadLink_1.7mm_Width_1.0mm, F.Cu at (146.0, 128.3)
- added REF**164: Pad_Link_1.7mm_Width_1.0mm, proto-pcb-silks:PadLink_1.7mm_Width_1.0mm, F.Cu at (148.6, 128.3)
- added REF**165: Pad_Link_1.7mm_Width_1.0mm, proto-pcb-silks:PadLink_1.7mm_Width_1.0mm, F.Cu at (151.1, 128.3)
- added REF**166: Pad_Link_1.7mm_Width_1.0mm, proto-pcb-silks:PadLink_1.7mm_Width_1.0mm, F.Cu at (153.6, 128.3)
- added REF**167: Pad_Link_1.7mm_Width_1.0mm, proto-pcb-silks:PadLink_1.7mm_Width_1.0mm, F.Cu at (156.2, 128.3)
- added REF**168: Pad_Link_1.7mm_Width_1.0mm, proto-pcb-silks:PadLink_1.7mm_Width_1.0mm, F.Cu at (158.7, 128.3)
- added REF**169: Pad_Link_1.7mm_Width_1.0mm, proto-pcb-silks:PadLink_1.7mm_Width_1.0mm, F.Cu at (161.3, 128.3)
- added REF**17: Pad_Link_1.7mm_Width_1.0mm, proto-pcb-silks:PadLink_1.7mm_Width_1.0mm, F.Cu at (156.2, 105.5)
- added REF**170: Pad_Link_1.7mm_Width_1.0mm, proto-pcb-silks:PadLink_1.7mm_Width_1.0mm, F.Cu at (163.8, 128.3)
- added REF**171: Pad_Link_1.7mm_Width_1.0mm, proto-pcb-silks:PadLink_1.7mm_Width_1.0mm, F.Cu at (166.3, 128.3)
- added REF**172: Pad_Link_1.7mm_Width_1.0mm, proto-pcb-silks:PadLink_1.7mm_Width_1.0mm, F.Cu at (168.9, 128.3)
- added REF**173: Pad_Link_1.7mm_Width_1.0mm, proto-pcb-silks:PadLink_1.7mm_Width_1.0mm, F.Cu at (113.0, 130.8)
- added REF**174: Pad_Link_1.7mm_Width_1.0mm, proto-pcb-silks:PadLink_1.7mm_Width_1.0mm, F.Cu at (115.5, 130.8)
- added REF**175: Pad_Link_1.7mm_Width_1.0mm, proto-pcb-silks:PadLink_1.7mm_Width_1.0mm, F.Cu at (118.1, 130.8)
- added REF**176: Pad_Link_1.7mm_Width_1.0mm, proto-pcb-silks:PadLink_1.7mm_Width_1.0mm, F.Cu at (120.6, 130.8)
- added REF**177: Pad_Link_1.7mm_Width_1.0mm, proto-pcb-silks:PadLink_1.7mm_Width_1.0mm, F.Cu at (123.2, 130.8)
- added REF**178: Pad_Link_1.7mm_Width_1.0mm, proto-pcb-silks:PadLink_1.7mm_Width_1.0mm, F.Cu at (125.7, 130.8)
- added REF**179: Pad_Link_1.7mm_Width_1.0mm, proto-pcb-silks:PadLink_1.7mm_Width_1.0mm, F.Cu at (128.2, 130.8)
- added REF**18: Pad_Link_1.7mm_Width_1.0mm, proto-pcb-silks:PadLink_1.7mm_Width_1.0mm, F.Cu at (158.7, 105.5)
- added REF**180: Pad_Link_1.7mm_Width_1.0mm, proto-pcb-silks:PadLink_1.7mm_Width_1.0mm, F.Cu at (130.8, 130.8)
- added REF**181: Pad_Link_1.7mm_Width_1.0mm, proto-pcb-silks:PadLink_1.7mm_Width_1.0mm, F.Cu at (133.3, 130.8)
- added REF**182: Pad_Link_1.7mm_Width_1.0mm, proto-pcb-silks:PadLink_1.7mm_Width_1.0mm, F.Cu at (135.9, 130.8)
- added REF**183: Pad_Link_1.7mm_Width_1.0mm, proto-pcb-silks:PadLink_1.7mm_Width_1.0mm, F.Cu at (138.4, 130.8)
- added REF**184: Pad_Link_1.7mm_Width_1.0mm, proto-pcb-silks:PadLink_1.7mm_Width_1.0mm, F.Cu at (140.9, 130.8)
- added REF**185: Pad_Link_1.7mm_Width_1.0mm, proto-pcb-silks:PadLink_1.7mm_Width_1.0mm, F.Cu at (143.5, 130.8)
- added REF**186: Pad_Link_1.7mm_Width_1.0mm, proto-pcb-silks:PadLink_1.7mm_Width_1.0mm, F.Cu at (146.0, 130.8)
- added REF**187: Pad_Link_1.7mm_Width_1.0mm, proto-pcb-silks:PadLink_1.7mm_Width_1.0mm, F.Cu at (148.6, 130.8)
- added REF**188: Pad_Link_1.7mm_Width_1.0mm, proto-pcb-silks:PadLink_1.7mm_Width_1.0mm, F.Cu at (151.1, 130.8)
- added REF**189: Pad_Link_1.7mm_Width_1.0mm, proto-pcb-silks:PadLink_1.7mm_Width_1.0mm, F.Cu at (153.6, 130.8)
- added REF**19: Pad_Link_1.7mm_Width_1.0mm, proto-pcb-silks:PadLink_1.7mm_Width_1.0mm, F.Cu at (161.3, 105.5)
- added REF**190: Pad_Link_1.7mm_Width_1.0mm, proto-pcb-silks:PadLink_1.7mm_Width_1.0mm, F.Cu at (156.2, 130.8)
- added REF**191: Pad_Link_1.7mm_Width_1.0mm, proto-pcb-silks:PadLink_1.7mm_Width_1.0mm, F.Cu at (158.7, 130.8)
- added REF**192: Pad_Link_1.7mm_Width_1.0mm, proto-pcb-silks:PadLink_1.7mm_Width_1.0mm, F.Cu at (161.3, 130.8)
- added REF**193: Pad_Link_1.7mm_Width_1.0mm, proto-pcb-silks:PadLink_1.7mm_Width_1.0mm, F.Cu at (163.8, 130.8)
- added REF**194: Pad_Link_1.7mm_Width_1.0mm, proto-pcb-silks:PadLink_1.7mm_Width_1.0mm, F.Cu at (166.3, 130.8)
- added REF**195: Pad_Link_1.7mm_Width_1.0mm, proto-pcb-silks:PadLink_1.7mm_Width_1.0mm, F.Cu at (168.9, 130.8)
- added REF**196: Pad_Link_1.7mm_Width_1.0mm, proto-pcb-silks:PadLink_1.7mm_Width_1.0mm, F.Cu at (113.0, 133.4)
- added REF**197: Pad_Link_1.7mm_Width_1.0mm, proto-pcb-silks:PadLink_1.7mm_Width_1.0mm, F.Cu at (115.5, 133.4)
- added REF**198: Pad_Link_1.7mm_Width_1.0mm, proto-pcb-silks:PadLink_1.7mm_Width_1.0mm, F.Cu at (118.1, 133.4)
- added REF**199: Pad_Link_1.7mm_Width_1.0mm, proto-pcb-silks:PadLink_1.7mm_Width_1.0mm, F.Cu at (120.6, 133.4)
- added REF**2: Pad_Link_1.7mm_Width_1.0mm, proto-pcb-silks:PadLink_1.7mm_Width_1.0mm, F.Cu at (118.1, 105.5)
- added REF**20: Pad_Link_1.7mm_Width_1.0mm, proto-pcb-silks:PadLink_1.7mm_Width_1.0mm, F.Cu at (113.0, 108.0)
- added REF**200: Pad_Link_1.7mm_Width_1.0mm, proto-pcb-silks:PadLink_1.7mm_Width_1.0mm, F.Cu at (123.2, 133.4)
- added REF**201: Pad_Link_1.7mm_Width_1.0mm, proto-pcb-silks:PadLink_1.7mm_Width_1.0mm, F.Cu at (125.7, 133.4)
- added REF**202: Pad_Link_1.7mm_Width_1.0mm, proto-pcb-silks:PadLink_1.7mm_Width_1.0mm, F.Cu at (128.2, 133.4)
- added REF**203: Pad_Link_1.7mm_Width_1.0mm, proto-pcb-silks:PadLink_1.7mm_Width_1.0mm, F.Cu at (130.8, 133.4)
- added REF**204: Pad_Link_1.7mm_Width_1.0mm, proto-pcb-silks:PadLink_1.7mm_Width_1.0mm, F.Cu at (133.3, 133.4)
- added REF**205: Pad_Link_1.7mm_Width_1.0mm, proto-pcb-silks:PadLink_1.7mm_Width_1.0mm, F.Cu at (135.9, 133.4)
- added REF**206: Pad_Link_1.7mm_Width_1.0mm, proto-pcb-silks:PadLink_1.7mm_Width_1.0mm, F.Cu at (138.4, 133.4)
- added REF**207: Pad_Link_1.7mm_Width_1.0mm, proto-pcb-silks:PadLink_1.7mm_Width_1.0mm, F.Cu at (140.9, 133.4)
- added REF**208: Pad_Link_1.7mm_Width_1.0mm, proto-pcb-silks:PadLink_1.7mm_Width_1.0mm, F.Cu at (143.5, 133.4)
- added REF**209: Pad_Link_1.7mm_Width_1.0mm, proto-pcb-silks:PadLink_1.7mm_Width_1.0mm, F.Cu at (146.0, 133.4)
- added REF**21: Pad_Link_1.7mm_Width_1.0mm, proto-pcb-silks:PadLink_1.7mm_Width_1.0mm, F.Cu at (115.5, 108.0)
- added REF**210: Pad_Link_1.7mm_Width_1.0mm, proto-pcb-silks:PadLink_1.7mm_Width_1.0mm, F.Cu at (148.6, 133.4)
- added REF**211: Pad_Link_1.7mm_Width_1.0mm, proto-pcb-silks:PadLink_1.7mm_Width_1.0mm, F.Cu at (151.1, 133.4)
- added REF**212: Pad_Link_1.7mm_Width_1.0mm, proto-pcb-silks:PadLink_1.7mm_Width_1.0mm, F.Cu at (153.6, 133.4)
- added REF**213: Pad_Link_1.7mm_Width_1.0mm, proto-pcb-silks:PadLink_1.7mm_Width_1.0mm, F.Cu at (156.2, 133.4)
- added REF**214: Pad_Link_1.7mm_Width_1.0mm, proto-pcb-silks:PadLink_1.7mm_Width_1.0mm, F.Cu at (158.7, 133.4)
- added REF**215: Pad_Link_1.7mm_Width_1.0mm, proto-pcb-silks:PadLink_1.7mm_Width_1.0mm, F.Cu at (161.3, 133.4)
- added REF**216: Pad_Link_1.7mm_Width_1.0mm, proto-pcb-silks:PadLink_1.7mm_Width_1.0mm, F.Cu at (163.8, 133.4)
- added REF**217: Pad_Link_1.7mm_Width_1.0mm, proto-pcb-silks:PadLink_1.7mm_Width_1.0mm, F.Cu at (166.3, 133.4)
- added REF**218: Pad_Link_1.7mm_Width_1.0mm, proto-pcb-silks:PadLink_1.7mm_Width_1.0mm, F.Cu at (168.9, 133.4)
- added REF**219: Pad_Link_1.7mm_Width_1.0mm, proto-pcb-silks:PadLink_1.7mm_Width_1.0mm, F.Cu at (113.0, 135.9)
- added REF**22: Pad_Link_1.7mm_Width_1.0mm, proto-pcb-silks:PadLink_1.7mm_Width_1.0mm, F.Cu at (118.1, 108.0)
- added REF**220: Pad_Link_1.7mm_Width_1.0mm, proto-pcb-silks:PadLink_1.7mm_Width_1.0mm, F.Cu at (115.5, 135.9)
- added REF**221: Pad_Link_1.7mm_Width_1.0mm, proto-pcb-silks:PadLink_1.7mm_Width_1.0mm, F.Cu at (118.1, 135.9)
- added REF**222: Pad_Link_1.7mm_Width_1.0mm, proto-pcb-silks:PadLink_1.7mm_Width_1.0mm, F.Cu at (120.6, 135.9)
- added REF**223: Pad_Link_1.7mm_Width_1.0mm, proto-pcb-silks:PadLink_1.7mm_Width_1.0mm, F.Cu at (123.2, 135.9)
- added REF**224: Pad_Link_1.7mm_Width_1.0mm, proto-pcb-silks:PadLink_1.7mm_Width_1.0mm, F.Cu at (125.7, 135.9)
- added REF**225: Pad_Link_1.7mm_Width_1.0mm, proto-pcb-silks:PadLink_1.7mm_Width_1.0mm, F.Cu at (128.2, 135.9)
- added REF**226: Pad_Link_1.7mm_Width_1.0mm, proto-pcb-silks:PadLink_1.7mm_Width_1.0mm, F.Cu at (130.8, 135.9)
- added REF**227: Pad_Link_1.7mm_Width_1.0mm, proto-pcb-silks:PadLink_1.7mm_Width_1.0mm, F.Cu at (133.3, 135.9)
- added REF**228: Pad_Link_1.7mm_Width_1.0mm, proto-pcb-silks:PadLink_1.7mm_Width_1.0mm, F.Cu at (135.9, 135.9)
- added REF**229: Pad_Link_1.7mm_Width_1.0mm, proto-pcb-silks:PadLink_1.7mm_Width_1.0mm, F.Cu at (138.4, 135.9)
- added REF**23: Pad_Link_1.7mm_Width_1.0mm, proto-pcb-silks:PadLink_1.7mm_Width_1.0mm, F.Cu at (120.6, 108.0)
- added REF**230: Pad_Link_1.7mm_Width_1.0mm, proto-pcb-silks:PadLink_1.7mm_Width_1.0mm, F.Cu at (140.9, 135.9)
- added REF**231: Pad_Link_1.7mm_Width_1.0mm, proto-pcb-silks:PadLink_1.7mm_Width_1.0mm, F.Cu at (143.5, 135.9)
- added REF**232: Pad_Link_1.7mm_Width_1.0mm, proto-pcb-silks:PadLink_1.7mm_Width_1.0mm, F.Cu at (146.0, 135.9)
- added REF**233: Pad_Link_1.7mm_Width_1.0mm, proto-pcb-silks:PadLink_1.7mm_Width_1.0mm, F.Cu at (148.6, 135.9)
- added REF**234: Pad_Link_1.7mm_Width_1.0mm, proto-pcb-silks:PadLink_1.7mm_Width_1.0mm, F.Cu at (151.1, 135.9)
- added REF**235: Pad_Link_1.7mm_Width_1.0mm, proto-pcb-silks:PadLink_1.7mm_Width_1.0mm, F.Cu at (153.6, 135.9)
- added REF**236: Pad_Link_1.7mm_Width_1.0mm, proto-pcb-silks:PadLink_1.7mm_Width_1.0mm, F.Cu at (156.2, 135.9)
- added REF**237: Pad_Link_1.7mm_Width_1.0mm, proto-pcb-silks:PadLink_1.7mm_Width_1.0mm, F.Cu at (158.7, 135.9)
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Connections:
- net Net-(J3-Pin_1) renamed GND
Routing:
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- added copper zone on B.Cu, net GND
- added copper zone on F.Cu, net GND
